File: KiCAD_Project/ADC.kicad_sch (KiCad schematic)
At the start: 16 parts, among them U4 1-0001530, U5 1-0001542

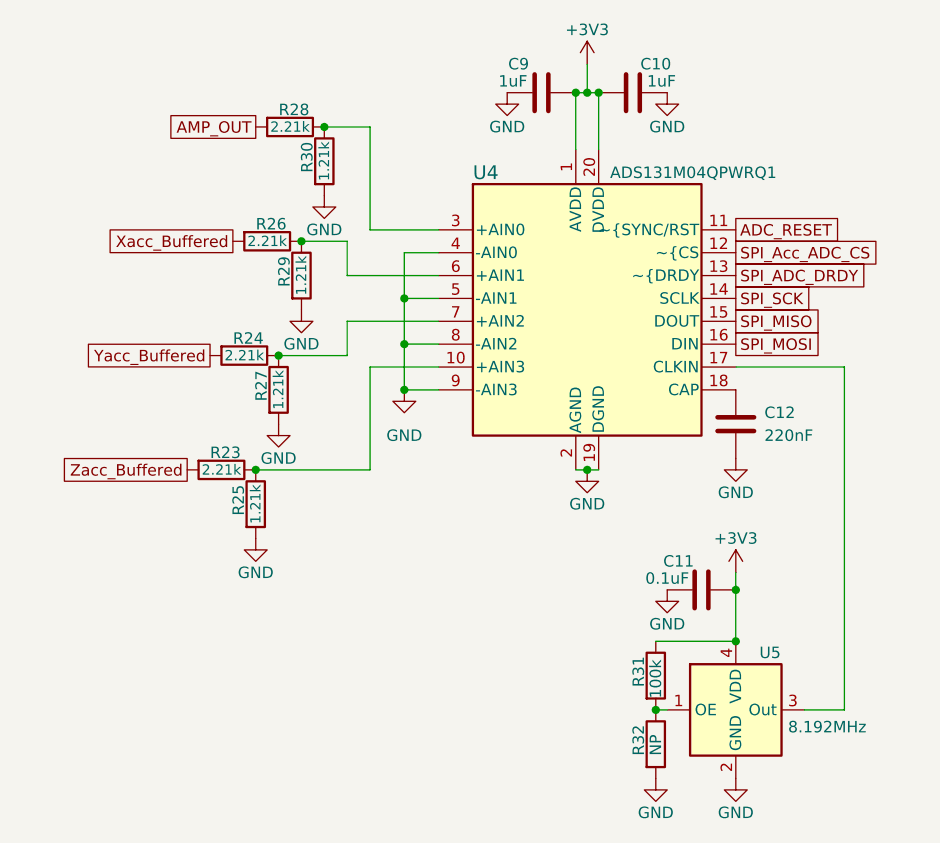
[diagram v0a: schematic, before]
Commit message: Rev 2.1 Changes: - Fixed Issue #11 (U4 Footprint pin 1 indicator) - Added Open Log Header for breakout - Removed SD Circuit - Connected GPS to I2C - Updated IPN and Revision Number
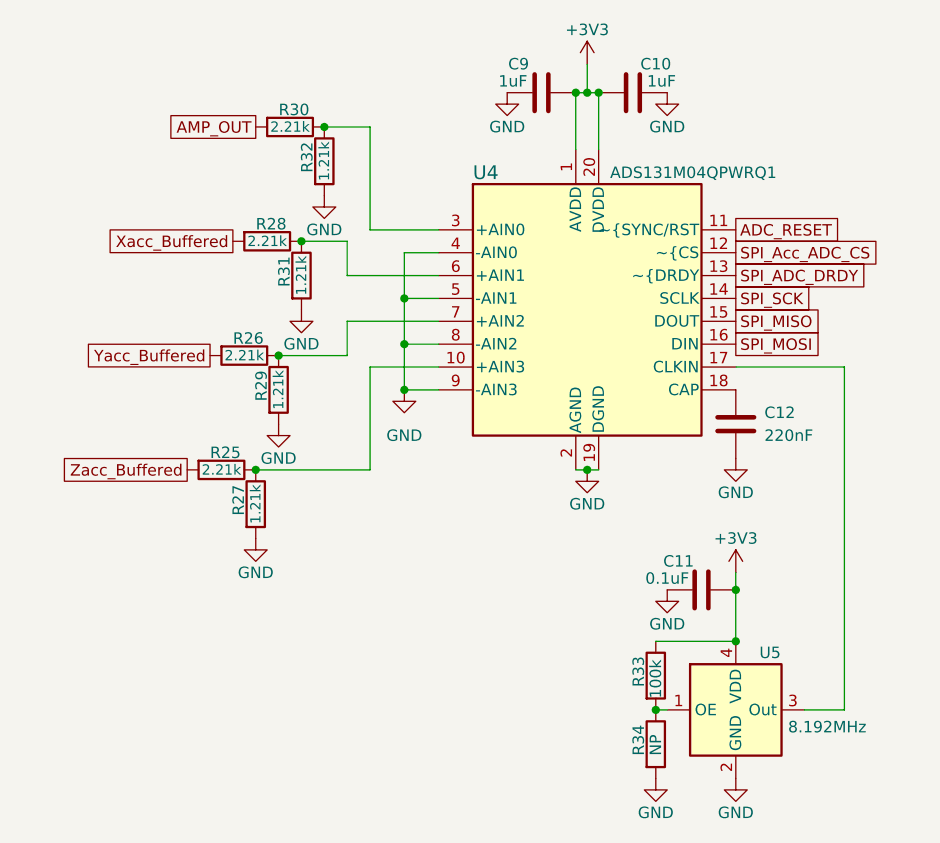
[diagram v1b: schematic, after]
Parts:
- renumbered R23 to R25, R24 to R26, R25 to R27, R26 to R28, R27 to R29, R28 to R30, R29 to R31, R30 to R32, R31 to R33, R32 to R34
